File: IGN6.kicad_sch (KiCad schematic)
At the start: 12 parts

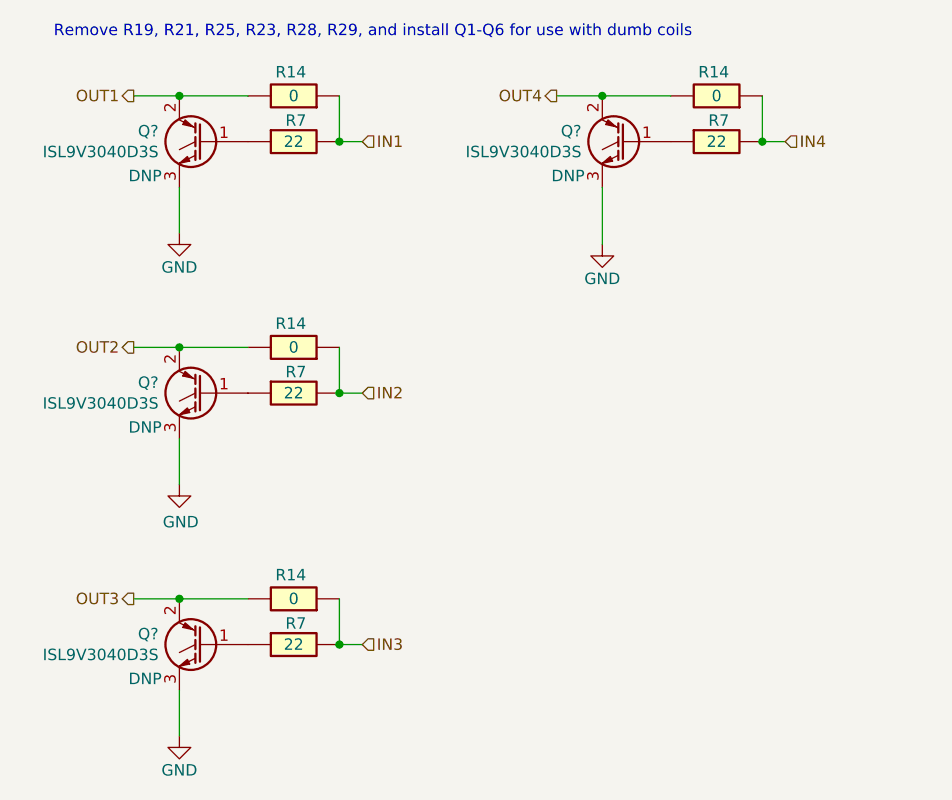
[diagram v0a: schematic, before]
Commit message: removed DNP from ignition drivers
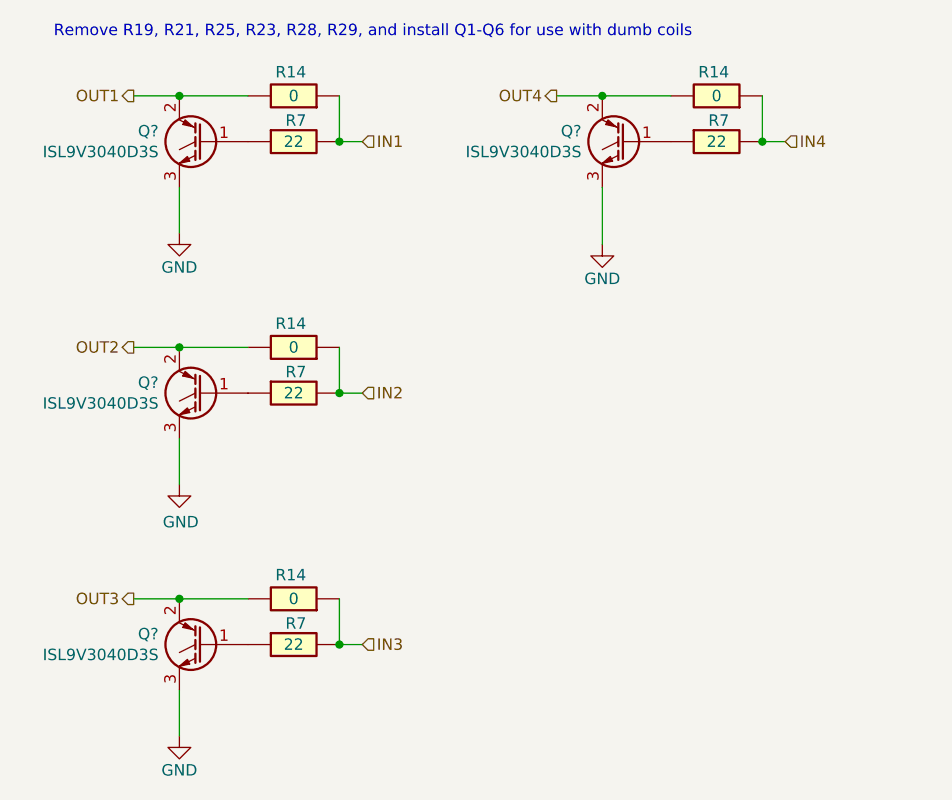
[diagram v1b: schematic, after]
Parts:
- Q? (x4): MyComment DNP -> (none)
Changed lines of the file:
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@@
       (effects (font (size 1.27 1.27)) hide)
     )
-    (property "MyComment" "DNP" (at 114.3 129.54 0)
+    (property "MyComment" "" (at 114.3 129.54 0)
       (effects (font (size 1.27 1.27)))
     )
@@
       (effects (font (size 1.27 1.27)) hide)
     )
-    (property "MyComment" "DNP" (at 114.3 73.66 0)
+    (property "MyComment" "" (at 114.3 73.66 0)
       (effects (font (size 1.27 1.27)))
     )
@@
       (effects (font (size 1.27 1.27)) hide)
     )
-    (property "MyComment" "DNP" (at 114.3 101.6 0)
+    (property "MyComment" "" (at 114.3 101.6 0)
       (effects (font (size 1.27 1.27)))
     )
@@
       (effects (font (size 1.27 1.27)) hide)
     )
-    (property "MyComment" "DNP" (at 161.29 73.66 0)
-      (effects (font (size 1.27 1.27)))
-    )
+    (property "MyComment" "" (at 161.29 73.66 0)
+      (effects (font (size 1.27 1.27)))
+    )
